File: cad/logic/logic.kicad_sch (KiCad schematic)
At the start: 15 parts, among them J1 Conn_01x06, J2 Conn_01x02, J3 Conn_01x02, J4 Conn_01x02, J5 Conn_01x02, J6 Conn_01x02, J7 Conn_01x02, J8 Conn_01x02, J9 Conn_01x02, U1 74HC595, U2 TPL7407LAD, U3 TPL7407LAD, U4 TPL7407LAD

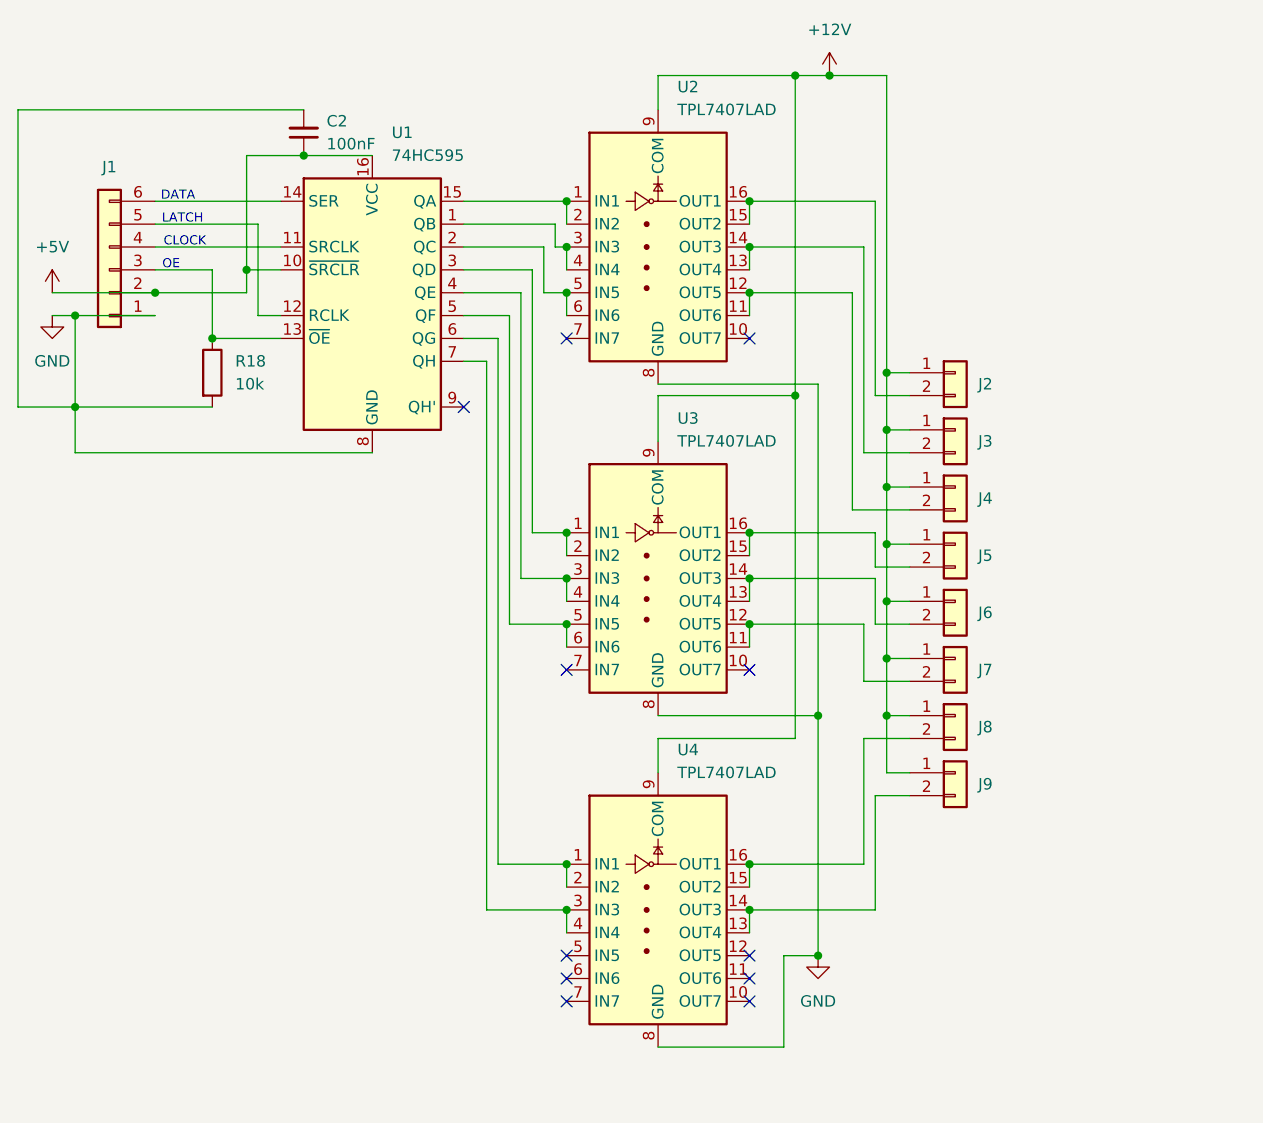
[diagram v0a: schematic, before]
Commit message: Simplified schema and wired PCB
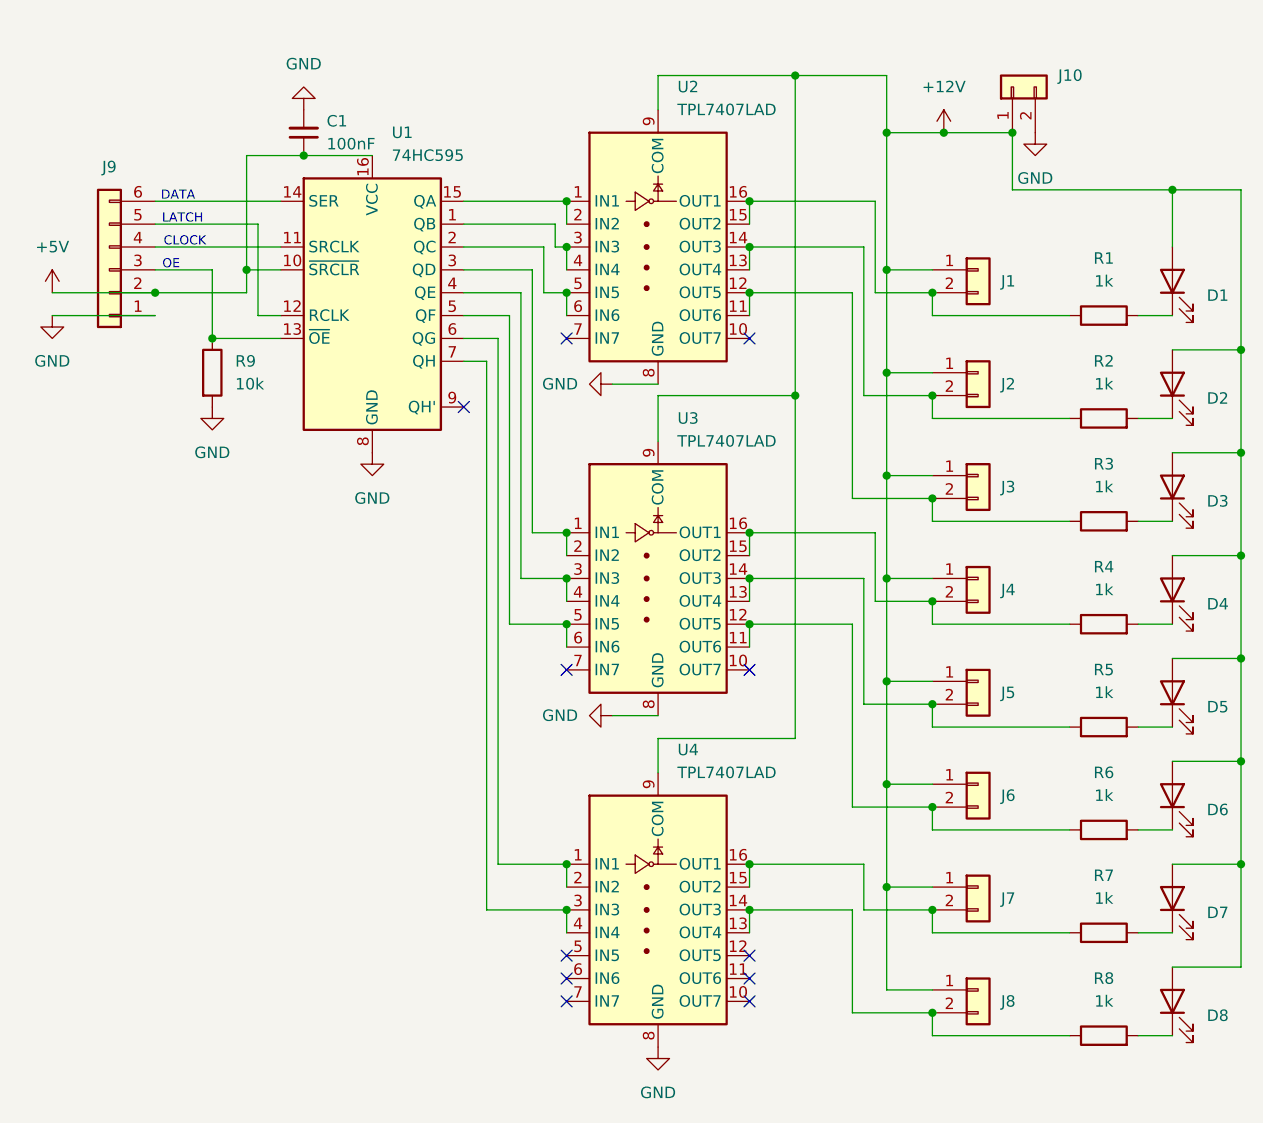
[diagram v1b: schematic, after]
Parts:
- added D1, D2, D3, D4, D5, D6, D7, D8: LED, LED_THT:LED_D3.0mm, symbol Device:LED
- added J10: Conn_01x02, Connector_JST:JST_PH_B2B-PH-K_1x02_P2.00mm_Vertical, symbol Connector_Generic:Conn_01x02
- added R1, R2, R3, R4, R5, R6, R7, R8: 1k, Resistor_THT:R_Axial_DIN0207_L6.3mm_D2.5mm_P7.62mm_Horizontal, symbol Device:R
- renumbered C2 to C1, J2 to J1, J3 to J2, J4 to J3, J5 to J4, J6 to J5, J7 to J6, J8 to J7, J9 to J8, J1 to J9, R18 to R9
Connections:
- net +12V: now also D1.2 (A), D2.2 (A), D3.2 (A), D4.2 (A), D5.2 (A), D6.2 (A), D7.2 (A), D8.2 (A), J10.1 (Pin_1)
- net GND: now also J10.2 (Pin_2)
- net at J6.2 (Pin_2), U3.11 (OUT6), U3.12 (OUT5): now also R6.1
- net at J5.2 (Pin_2), U3.13 (OUT4), U3.14 (OUT3): now also R5.1
- net at J4.2 (Pin_2), U3.15 (OUT2), U3.16 (OUT1): now also R4.1
- net at J3.2 (Pin_2), U2.11 (OUT6), U2.12 (OUT5): now also R3.1
- net at J2.2 (Pin_2), U2.13 (OUT4), U2.14 (OUT3): now also R2.1
- net at J1.2 (Pin_2), U2.15 (OUT2), U2.16 (OUT1): now also R1.1
- net at J7.2 (Pin_2), U4.15 (OUT2), U4.16 (OUT1): now also R7.1
- net at J8.2 (Pin_2), U4.13 (OUT4), U4.14 (OUT3): now also R8.1
- new net: D6.1 (K), R6.2
- new net: D2.1 (K), R2.2
- new net: D5.1 (K), R5.2
- new net: D3.1 (K), R3.2
- new net: D8.1 (K), R8.2
- new net: D4.1 (K), R4.2
- new net: D7.1 (K), R7.2
- new net: D1.1 (K), R1.2
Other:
- moved on the sheet: J1, J2, J3, J4, J5, J6, J7, J8

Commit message: Initial design complete
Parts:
- removed J10: Conn_01x02, Connector_JST:JST_PH_B2B-PH-K_1x02_P2.00mm_Vertical, symbol Connector_Generic:Conn_01x02
- removed J9: Conn_01x06, Connector_JST:JST_PH_B6B-PH-K_1x06_P2.00mm_Vertical, symbol Connector_Generic:Conn_01x06
- removed U1: 74HC595, Package_DIP:DIP-16_W7.62mm_Socket, symbol 74xx:74HC595
- removed U2, U3, U4: TPL7407LAD, Package_SO:SOIC-16_3.9x9.9mm_P1.27mm, symbol Transistor_Array:TPL7407LAD
- added A1: Arduino_Nano_ESP32, Module:Arduino_Nano, symbol MCU_Module:Arduino_Nano_ESP32
- added C2, C3, C4: 100nF, Capacitor_THT:C_Disc_D4.7mm_W2.5mm_P5.00mm, symbol Device:C_Small
- added J10, J11, J12, J13, J14, J15, J16, J17: Conn_01x04, Connector_JST:JST_PH_B4B-PH-K_1x04_P2.00mm_Vertical, symbol Connector_Generic:Conn_01x04
- added J9: Barrel_Jack_Switch, Connector_BarrelJack:BarrelJack_Horizontal, symbol Connector:Barrel_Jack_Switch
- added R10, R11: 100R, Resistor_THT:R_Axial_DIN0207_L6.3mm_D2.5mm_P7.62mm_Horizontal, symbol Device:R
- added U1: R-78E5.0-1.0, Converter_DCDC:Converter_DCDC_RECOM_R-78E-0.5_THT, symbol Regulator_Switching:R-78E5.0-1.0
- added U2: 74HC595, Package_DIP:DIP-16_W7.62mm_Socket, symbol 74xx:74HC595
- added U3: TBD62381APG, footprints:P-DIP18-300-2p54-001_TOS, symbol watersystem:TBD62381APG
- added U4: TCA9548APWR, Package_DIP:DIP-24_18.0mmx34.29mm_W15.24mm_Socket, symbol Interface_Expansion:TCA9548APWR
- C1: footprint Capacitor_SMD:C_0805_2012Metric_Pad1.18x1.45mm_HandSolder -> Capacitor_THT:C_Disc_D4.7mm_W2.5mm_P5.00mm
- R1, R2, R3: value 1k -> 10k
- R4, R5, R6, R7, R8: value 1k -> 100R
- R9: value 10k -> 100R
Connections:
- net +12V: now also R4.2, R5.2, R6.2, R7.2, R8.2, R9.2, A1.30 (VIN), C4.1, J9.1, R10.2, R11.2, U1.1 (IN); no longer D1.2 (A), D2.2 (A), D3.2 (A), D4.2 (A), D5.2 (A), D6.2 (A), D7.2 (A), D8.2 (A)
- net +5V: now also R2.2, R3.2, C2.1, C3.1, J10.3 (Pin_3), J11.3 (Pin_3), J12.3 (Pin_3), J13.3 (Pin_3), J14.3 (Pin_3), J15.3 (Pin_3), J16.3 (Pin_3), J17.3 (Pin_3), U1.3 (OUT), U2.16 (VCC), U3.10 (VCC), U4.24 (VCC)
- net GND: now also R1.2, A1.29 (GND), A1.4 (GND), C2.2, C3.2, C4.2, J10.4 (Pin_4), J11.4 (Pin_4), J12.4 (Pin_4), J13.4 (Pin_4), J14.4 (Pin_4), J15.4 (Pin_4), J16.4 (Pin_4), J17.4 (Pin_4), J9.2, U1.2 (GND), U2.8 (GND), U3.9 (GND), U4.12 (GND); no longer R9.2
- net at D6.1 (K): now also J6.2 (Pin_2), U3.13 (O6); no longer R6.2
- net at D2.1 (K): now also J2.2 (Pin_2), U3.17 (O2); no longer R2.2
- net at R6.1: now also D3.2 (A); no longer J6.2 (Pin_2)
- net at R5.1: now also D2.2 (A); no longer J5.2 (Pin_2)
- net at J4.2 (Pin_2): now also D4.1 (K), U3.15 (O4); no longer R4.1
- net at D5.1 (K): now also J5.2 (Pin_2), U3.14 (O5); no longer R5.2
- net at R3.1: now also A1.10 (D7), U4.3 (~{RESET}); no longer J3.2 (Pin_2)
- net at R2.1: now also A1.5 (D2), U2.10 (~{SRCLR}); no longer J2.2 (Pin_2)
- net at R1.1: now also A1.8 (D5), U2.13 (~{OE}); no longer J1.2 (Pin_2)
- net at D3.1 (K): now also J3.2 (Pin_2), U3.16 (O3); no longer R3.2
- net at R9.1: now also D6.2 (A)
- net at J7.2 (Pin_2): now also D7.1 (K), U3.12 (O7); no longer R7.1
- net at J8.2 (Pin_2): now also D8.1 (K), U3.11 (O8); no longer R8.1
- net at D1.1 (K): now also J1.2 (Pin_2), U3.18 (O1); no longer R1.2
- new net: D7.2 (A), R10.1
- new net: D5.2 (A), R8.1
- new net: J13.2 (Pin_2), U4.10 (SD3)
- new net: J13.1 (Pin_1), U4.11 (SC3)
- new net: J14.2 (Pin_2), U4.13 (SD4)
- new net: J14.1 (Pin_1), U4.14 (SC4)
- new net: J15.2 (Pin_2), U4.15 (SD5)
- new net: J15.1 (Pin_1), U4.16 (SC5)
- new net: J16.2 (Pin_2), U4.17 (SD6)
- new net: J16.1 (Pin_1), U4.18 (SC6)
- new net: J17.2 (Pin_2), U4.19 (SD7)
- new net: J17.1 (Pin_1), U4.20 (SC7)
- new net: A1.24 (SCL/A5), U4.22 (SCL)
- new net: A1.23 (SDA/A4), U4.23 (SDA)
- new net: J10.2 (Pin_2), U4.4 (SD0)
- new net: J10.1 (Pin_1), U4.5 (SC0)
- new net: J11.2 (Pin_2), U4.6 (SD1)
- new net: J11.1 (Pin_1), U4.7 (SC1)
- new net: J12.2 (Pin_2), U4.8 (SD2)
- new net: J12.1 (Pin_1), U4.9 (SC2)
- new net: A1.6 (D3), U2.11 (SRCLK)
- new net: A1.7 (D4), U2.12 (RCLK)
- new net: A1.9 (D6), U2.14 (SER)
- new net: U2.15 (QA), U3.1 (I1)
- new net: U2.1 (QB), U3.2 (I2)
- new net: U2.2 (QC), U3.3 (I3)
- new net: U2.3 (QD), U3.4 (I4)
- new net: U2.4 (QE), U3.5 (I5)
- new net: U2.5 (QF), U3.6 (I6)
- new net: U2.6 (QG), U3.7 (I7)
- new net: U2.7 (QH), U3.8 (I8)
- new net: D1.2 (A), R4.1
- new net: D8.2 (A), R11.1
- new net: D4.2 (A), R7.1
- no-connect marks 11 -> 2
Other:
- note removed: "CLOCK"
- note removed: "DATA"
- note removed: "LATCH"
- note removed: "OE"
- moved on the sheet: D1, J1

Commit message: Added capacitor
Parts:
- added C5: 20µF, Capacitor_THT:C_Disc_D4.7mm_W2.5mm_P5.00mm, symbol Device:C_Small
- U3: footprint footprints:P-DIP18-300-2p54-001_TOS -> Package_DIP:CERDIP-18_W7.62mm_SideBrazed_Socket
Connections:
- net +5V: now also C5.1
- net GND: now also C5.2
- no-connect marks 2 -> 24
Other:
- moved on the sheet: D1, D2, D3, D4, D5, D6, D7, D8, J1, J2, J3, J4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
